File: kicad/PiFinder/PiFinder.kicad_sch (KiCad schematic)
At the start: 43 parts, among them J1 Raspberry_Pi_2_3, J2 display, J3 IMU, Q1 Q_NPN_EBC, SW0 SW_Push_Dual, SW1 SW_Push_Dual, SW2 SW_Push_Dual, SW3 SW_Push_Dual, SW4 SW_Push_Dual, SW5 SW_Push_Dual, SW6 SW_Push_Dual, SW7 SW_Push_Dual, SW8 SW_Push_Dual, SW9 SW_Push_Dual

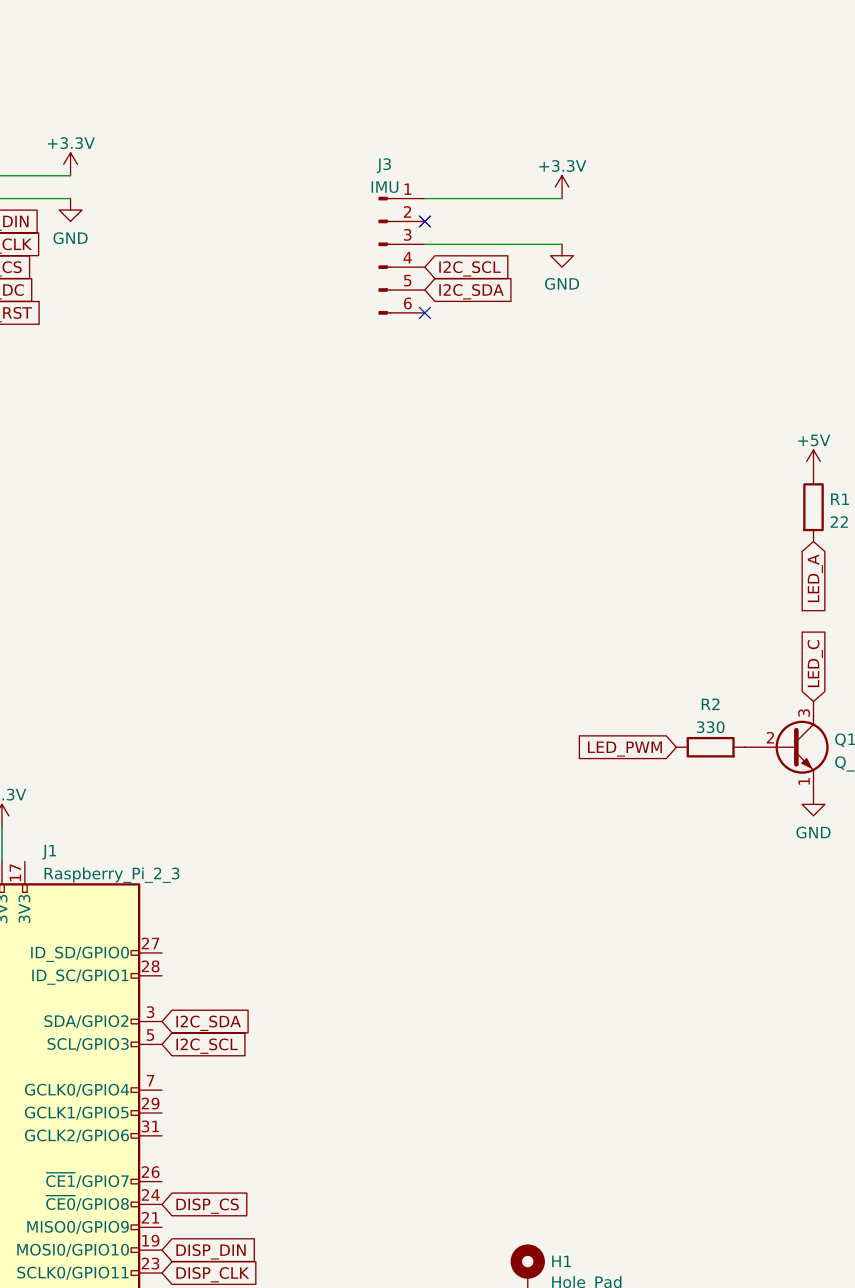
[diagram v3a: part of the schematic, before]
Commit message: Add version to PCB silkscreen
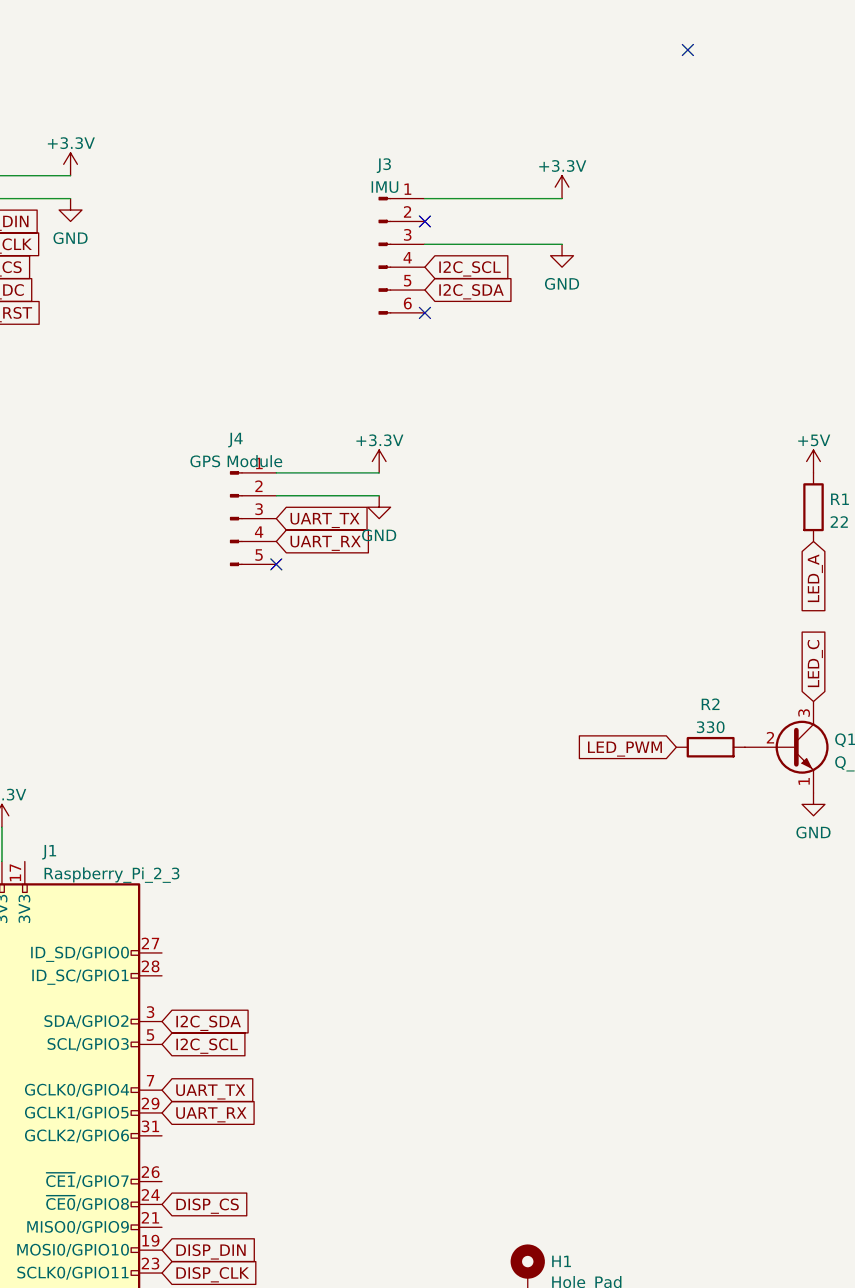
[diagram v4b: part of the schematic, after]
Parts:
- added J4: GPS Module, RSU:GT-U7_GPS, symbol Connector:Conn_01x05_Male
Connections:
- net +3.3V: now also J4.1 (Pin_1)
- net GND: now also J4.2 (Pin_2)
- net UART_RX: now reaches J1.29 (GCLK1/GPIO5)
- net UART_RX: now also J4.4 (Pin_4)
- net UART_TX: now reaches J1.7 (GCLK0/GPIO4)
- net UART_TX: now also J4.3 (Pin_3)
- no-connect marks 2 -> 4
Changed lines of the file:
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@@
   )
   (no_connect (at 99.06 53.34))
+  (no_connect (at 128.27 24.13))
+  (no_connect (at 82.55 81.28))
   (no_connect (at 99.06 43.18))
   (wire (pts (xy 209.55 113.03) (xy 252.73 113.03))
@@
     (stroke (width 0) (type default) (color 0 0 0 0))
   )
+  (wire (pts (xy 82.55 71.12) (xy 93.98 71.12))
+    (stroke (width 0) (type default) (color 0 0 0 0))
+  )
   (wire (pts (xy 194.31 39.37) (xy 215.9 39.37))
     (stroke (width 0) (type default) (color 0 0 0 0))
@@
     (stroke (width 0) (type default) (color 0 0 0 0))
   )
+  (wire (pts (xy 82.55 73.66) (xy 93.98 73.66))
+    (stroke (width 0) (type default) (color 0 0 0 0))
+  )
   (wire (pts (xy 240.03 29.21) (xy 240.03 36.83))
     (stroke (width 0) (type default) (color 0 0 0 0))
@@
     )
   )
+  (global_label "UART_TX" (shape input) (at 69.85 139.7 0) (fields_autoplaced)
+    (effects (font (size 1.27 1.27)) (justify left))
+    (property "Intersheet References" "${INTERSHEET_REFS}" (id 0) (at 79.9756 139.6206 0)
+      (effects (font (size 1.27 1.27)) (justify left) hide)
+    )
+  )
   (global_label "LED_PWM" (shape input) (at 127 101.6 180) (fields_autoplaced)
     (effects (font (size 1.27 1.27)) (justify right))
@@
     )
   )
+  (global_label "UART_TX" (shape input) (at 82.55 76.2 0) (fields_autoplaced)
+    (effects (font (size 1.27 1.27)) (justify left))
+    (property "Intersheet References" "${INTERSHEET_REFS}" (id 0) (at 92.6756 76.1206 0)
+      (effects (font (size 1.27 1.27)) (justify left) hide)
+    )
+  )
+  (global_label "UART_RX" (shape input) (at 82.55 78.74 0) (fields_autoplaced)
+    (effects (font (size 1.27 1.27)) (justify left))
+    (property "Intersheet References" "${INTERSHEET_REFS}" (id 0) (at 92.978 78.6606 0)
+      (effects (font (size 1.27 1.27)) (justify left) hide)
+    )
+  )
   (global_label "ROW1" (shape input) (at 173.99 60.96 180) (fields_autoplaced)
     (effects (font (size 1.27 1.27)) (justify right))
@@
     (effects (font (size 1.27 1.27)) (justify left))
     (property "Intersheet References" "${INTERSHEET_REFS}" (id 0) (at 56.5713 43.1006 0)
+      (effects (font (size 1.27 1.27)) (justify left) hide)
+    )
+  )
+  (global_label "UART_RX" (shape input) (at 69.85 142.24 0) (fields_autoplaced)
+    (effects (font (size 1.27 1.27)) (justify left))
+    (property "Intersheet References" "${INTERSHEET_REFS}" (id 0) (at 80.278 142.1606 0)
       (effects (font (size 1.27 1.27)) (justify left) hide)
     )
@@
     (pin "2")
   )
+  (symbol (lib_id "power:GND") (at 93.98 73.66 0) (unit 1)
+    (in_bom yes) (on_board yes) (fields_autoplaced)
+    (property "Reference" "#PWR0107" (id 0) (at 93.98 80.01 0)
+      (effects (font (size 1.27 1.27)) hide)
+    )
+    (property "Value" "GND" (id 1) (at 93.98 78.1034 0))
+    (property "Footprint" "" (id 2) (at 93.98 73.66 0)
+      (effects (font (size 1.27 1.27)) hide)
+    )
+    (property "Datasheet" "" (id 3) (at 93.98 73.66 0)
+      (effects (font (size 1.27 1.27)) hide)
+    )
+    (pin "1")
+  )
   (symbol (lib_id "Device:LED") (at 213.36 132.08 0) (unit 1)
     (in_bom yes) (on_board yes) (fields_autoplaced)
@@
     )
     (pin "1")
+  )
+  (symbol (lib_id "Connector:Conn_01x05_Male") (at 77.47 76.2 0) (unit 1)
+    (in_bom yes) (on_board yes) (fields_autoplaced)
+    (property "Reference" "J4" (id 0) (at 78.105 67.344 0))
+    (property "Value" "GPS Module" (id 1) (at 78.105 69.8809 0))
+    (property "Footprint" "RSU:GT-U7_GPS" (id 2) (at 77.47 76.2 0)
+      (effects (font (size 1.27 1.27)) hide)
+    )
+    (property "Datasheet" "~" (id 3) (at 77.47 76.2 0)
+      (effects (font (size 1.27 1.27)) hide)
+    )
+    (pin "1")
+    (pin "2")
+    (pin "3")
+    (pin "4")
+    (pin "5")
   )
   (symbol (lib_id "Device:LED") (at 257.81 132.08 0) (unit 1)
@@
     (pin "1")
     (pin "2")
+  )
+  (symbol (lib_id "power:+3.3V") (at 93.98 71.12 0) (unit 1)
+    (in_bom yes) (on_board yes) (fields_autoplaced)
+    (property "Reference" "#PWR0109" (id 0) (at 93.98 74.93 0)
+      (effects (font (size 1.27 1.27)) hide)
+    )
+    (property "Value" "+3.3V" (id 1) (at 93.98 67.5442 0))
+    (property "Footprint" "" (id 2) (at 93.98 71.12 0)
+      (effects (font (size 1.27 1.27)) hide)
+    )
+    (property "Datasheet" "" (id 3) (at 93.98 71.12 0)
+      (effects (font (size 1.27 1.27)) hide)
+    )
+    (pin "1")
   )
   (symbol (lib_id "power:GND") (at 59.69 40.64 0) (unit 1)
@@
       (reference "#PWR0106") (unit 1) (value "+3.3V") (footprint "")
     )
+    (path "/6e18660f-fedd-43fe-8168-4d1438fd3ba0"
+      (reference "#PWR0107") (unit 1) (value "GND") (footprint "")
+    )
     (path "/7eab7327-8e7d-4f71-a45d-d0dd3546a0a1"
       (reference "#PWR0108") (unit 1) (value "+5V") (footprint "")
     )
+    (path "/bd88f1da-18b0-4630-a917-2fcf90647e6d"
+      (reference "#PWR0109") (unit 1) (value "+3.3V") (footprint "")
+    )
     (path "/c6c12936-aadb-414c-a8d0-8fdfc38b1e14"
       (reference "#PWR0110") (unit 1) (value "+5V") (footprint "")
@@
       (reference "J3") (unit 1) (value "IMU") (footprint "RSU:Adafruit_BNO055_IMU")
     )
+    (path "/9215a07e-9819-4e3a-990a-11daa40ffae0"
+      (reference "J4") (unit 1) (value "GPS Module") (footprint "RSU:GT-U7_GPS")
+    )
     (path "/3c55eedc-d17b-4a97-ba37-d04b44ec1930"
